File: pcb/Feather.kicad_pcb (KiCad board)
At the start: 2 copper layers, 57 x 22.9 mm, 40 parts, among them J1 MicroUSB, J2 S2B-PH-SM4-TB, J3 ANT, J4 U.FL, J5 Conn_01x03, J6 Conn_01x12, J7 Conn_01x16, SW1 KMR2, U1 ATSAMD21G18A, U2 AP2112K-3.3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

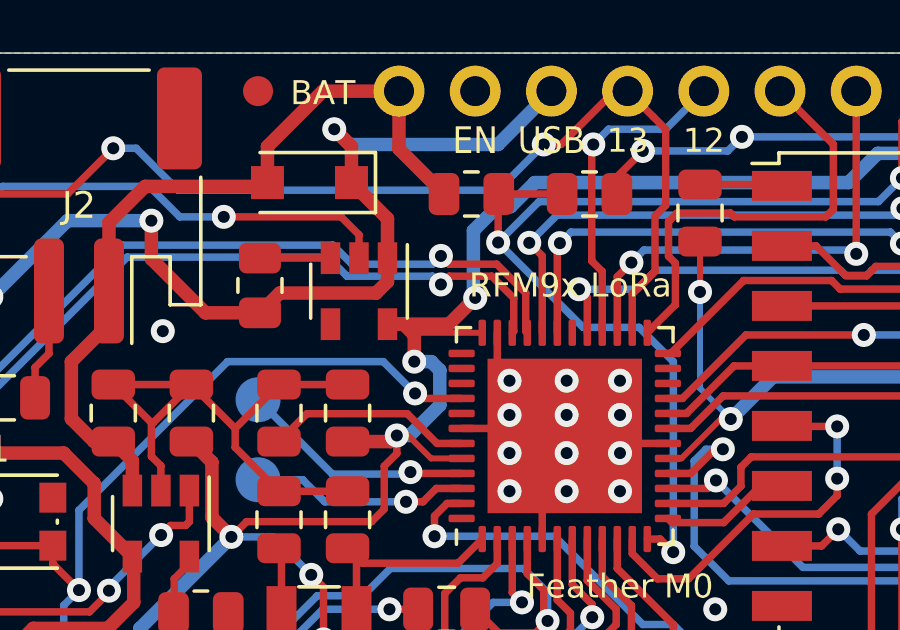
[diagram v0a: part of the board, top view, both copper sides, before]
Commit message: Leves ajustes en el texto aclaratorio del PCB.
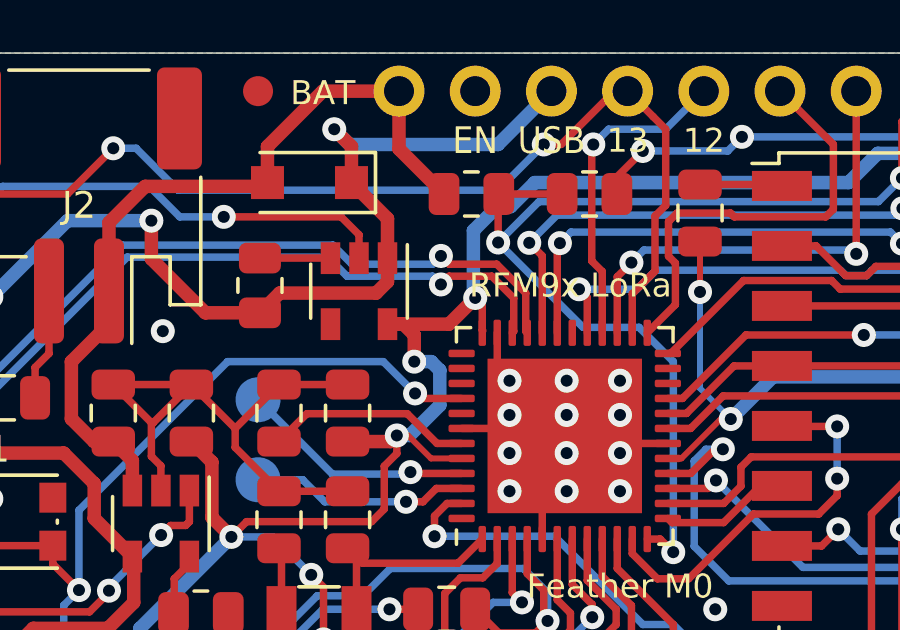
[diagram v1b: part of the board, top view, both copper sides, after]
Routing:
- net +3V3: track 115.0 -> 114.0 mm

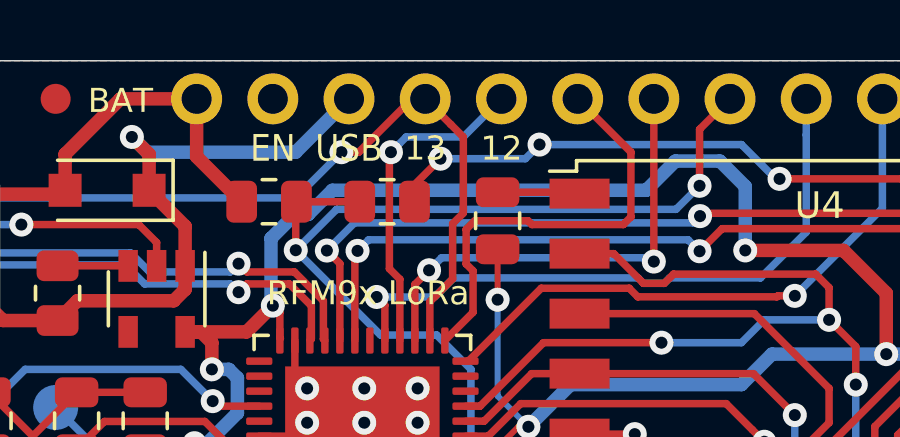
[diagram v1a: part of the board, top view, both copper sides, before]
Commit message: Se agregaron algunas regiones de 'keep out' en el cobre superior para mejorar la prolijidad del circuito.
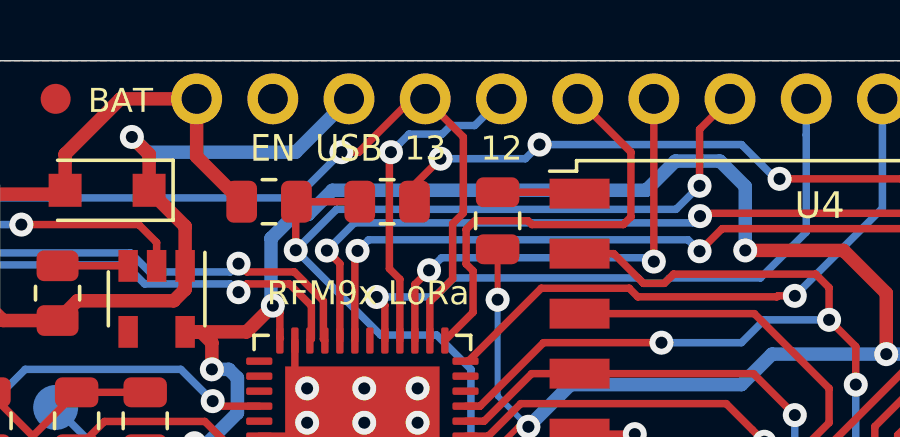
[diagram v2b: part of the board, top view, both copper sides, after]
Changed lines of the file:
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@@
     (thickness 1.6)
     (drawings 96)
-    (tracks 653)
+    (tracks 655)
     (zones 0)
     (modules 40)
@@
   (segment (start 143.33099 82.60201) (end 143.33099 86.43499) (width 0.25) (layer F.Cu) (net 27))
   (segment (start 143.383 82.55) (end 143.33099 82.60201) (width 0.25) (layer F.Cu) (net 27))
+  (segment (start 143.985999 81.947001) (end 143.637 82.296) (width 0.25) (layer B.Cu) (net 27))
   (segment (start 143.637 82.296) (end 143.383 82.55) (width 0.25) (layer B.Cu) (net 27))
-  (segment (start 143.891 82.042) (end 143.637 82.296) (width 0.25) (layer B.Cu) (net 27))
-  (segment (start 145.796 82.042) (end 143.891 82.042) (width 0.25) (layer B.Cu) (net 27))
-  (segment (start 147.066 80.772) (end 145.796 82.042) (width 0.25) (layer B.Cu) (net 27))
+  (segment (start 145.090001 81.947001) (end 143.985999 81.947001) (width 0.25) (layer B.Cu) (net 27))
+  (segment (start 145.376002 81.661) (end 145.090001 81.947001) (width 0.25) (layer B.Cu) (net 27))
+  (segment (start 146.177 81.661) (end 145.376002 81.661) (width 0.25) (layer B.Cu) (net 27))
+  (segment (start 147.066 80.772) (end 146.177 81.661) (width 0.25) (layer B.Cu) (net 27))
   (segment (start 120.142 81.0025) (end 120.4995 81.0025) (width 0.25) (layer F.Cu) (net 28))
   (segment (start 120.4995 81.0025) (end 121.412 81.915) (width 0.25) (layer F.Cu) (net 28))
@@
       )
     )
+  )
+  (zone (net 0) (net_name "") (layer F.Cu) (hatch edge 0.508)
+    (connect_pads (clearance 0.508))
+    (min_thickness 0.254)
+    (keepout (tracks allowed) (vias allowed) (copperpour not_allowed))
+    (fill (arc_segments 32) (thermal_gap 0.508) (thermal_bridge_width 0.508))
+    (polygon
+      (pts
+        (xy 144.653 85.725) (xy 143.764 85.725) (xy 143.764 84.836) (xy 144.653 84.836)
+      )
+    )
+  )
+  (zone (net 0) (net_name "") (layer F.Cu) (hatch edge 0.508)
+    (connect_pads (clearance 0.508))
+    (min_thickness 0.254)
+    (keepout (tracks allowed) (vias allowed) (copperpour not_allowed))
+    (fill (arc_segments 32) (thermal_gap 0.508) (thermal_bridge_width 0.508))
+    (polygon
+      (pts
+        (xy 145.288 83.185) (xy 144.145 83.185) (xy 144.145 82.042) (xy 145.288 82.042)
+      )
+    )
+  )
+  (zone (net 0) (net_name "") (layer F.Cu) (hatch edge 0.508)
+    (connect_pads (clearance 0.508))
+    (min_thickness 0.254)
+    (keepout (tracks allowed) (vias allowed) (copperpour not_allowed))
+    (fill (arc_segments 32) (thermal_gap 0.508) (thermal_bridge_width 0.508))
+    (polygon
+      (pts
+        (xy 170.053 95.123) (xy 170.053 96.012) (xy 168.656 96.012) (xy 168.656 94.869)
+      )
+    )
+  )
+  (zone (net 0) (net_name "") (layer F.Cu) (hatch edge 0.508)
+    (connect_pads (clearance 0.508))
+    (min_thickness 0.254)
+    (keepout (tracks allowed) (vias allowed) (copperpour not_allowed))
+    (fill (arc_segments 32) (thermal_gap 0.508) (thermal_bridge_width 0.508))
+    (polygon
+      (pts
+        (xy 126.746 84.836) (xy 125.857 84.836) (xy 127.254 83.566) (xy 128.016 83.566)
+      )
+    )
+  )
+  (zone (net 0) (net_name "") (layer F.Cu) (hatch edge 0.508)
+    (connect_pads (clearance 0.508))
+    (min_thickness 0.254)
+    (keepout (tracks allowed) (vias allowed) (copperpour not_allowed))
+    (fill (arc_segments 32) (thermal_gap 0.508) (thermal_bridge_width 0.508))
+    (polygon
+      (pts
+        (xy 131.953 97.028) (xy 130.683 97.028) (xy 130.683 96.393) (xy 131.953 96.393)
+      )
+    )

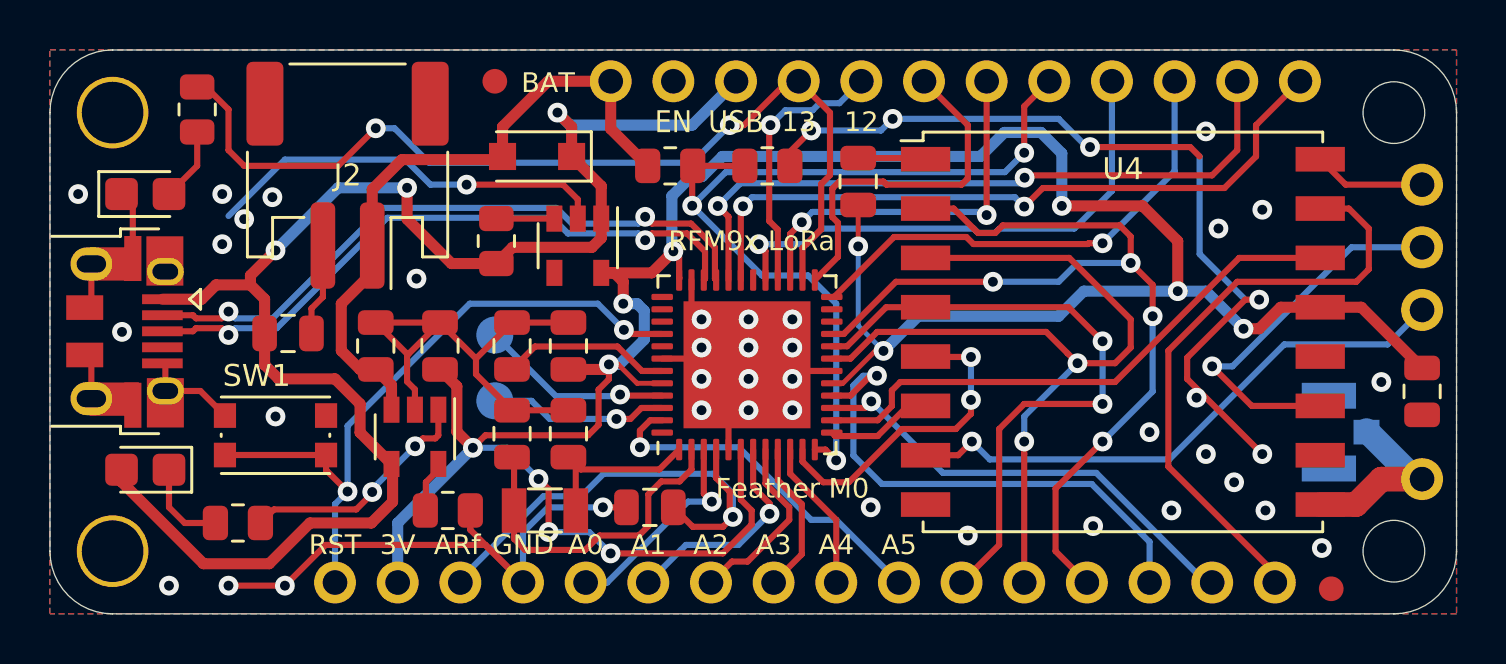
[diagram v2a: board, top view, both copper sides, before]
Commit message: Se realizaron ajustes a los 'keep outs' de la capa de cobre superior.
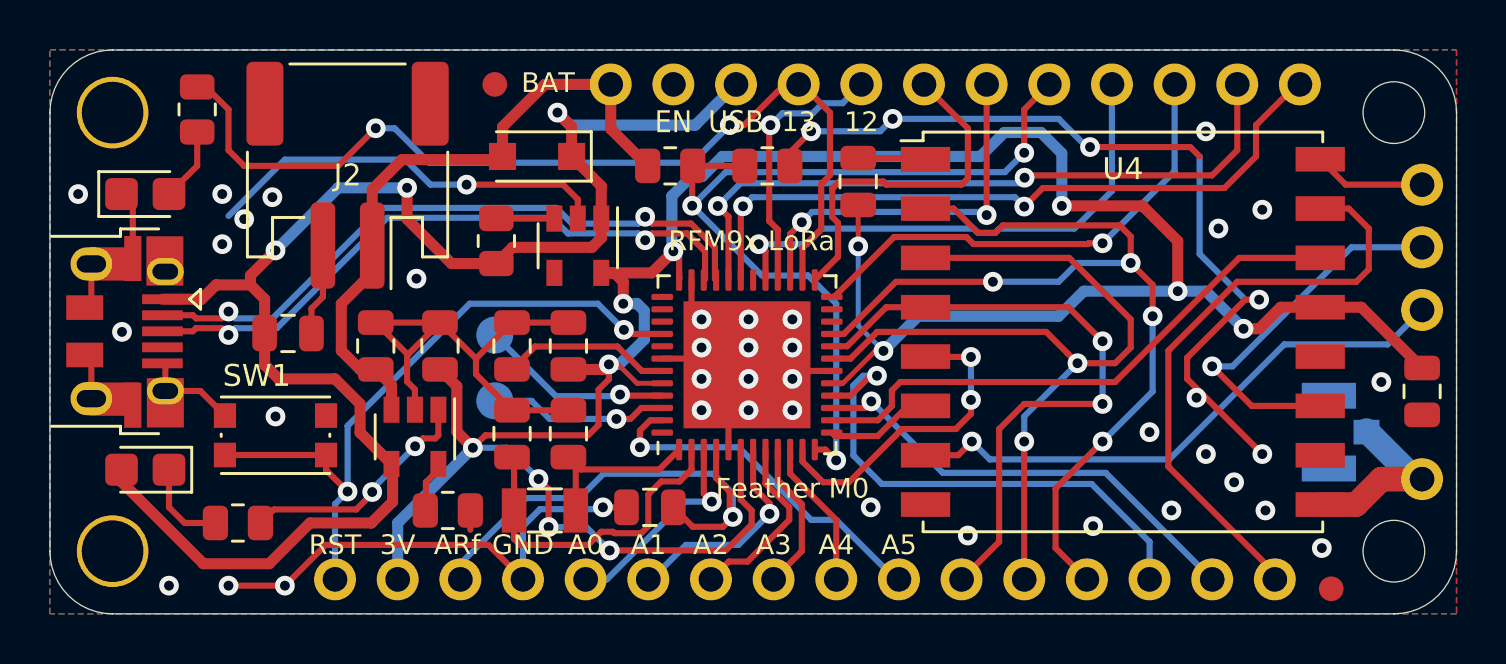
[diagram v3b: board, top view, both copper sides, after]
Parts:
- moved FID2 0.13 mm to (132.2, 80.9)
- moved J6 0.13 mm to (136.9, 80.9)
- moved J7 0.13 mm to (163.8, 101.0)
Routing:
- net GND: track 127.4 -> 124.6 mm
